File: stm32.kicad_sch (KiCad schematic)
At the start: 17 parts, among them J1 TC2030-IDC, U2 STM32F410CBU6, U3 RT9080-33GJ5

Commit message: more routing. switched to RA buttons, moved the buck closer to the barrel
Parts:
- removed C7, C8: 1uF, Capacitor_SMD:C_0402_1005Metric, symbol Device:C
- removed U3: RT9080-33GJ5, blockaxe:RT9080-33GJ5, symbol blockaxe:RT9080-33GJ5
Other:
- note removed: "STM32 3V3 LDO"
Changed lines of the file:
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@@
   (junction (at 63.5 67.945) (diameter 0) (color 0 0 0 0)
   )
-  (junction (at 73.025 24.13) (diameter 0) (color 0 0 0 0)
-  )
-  (junction (at 34.925 24.13) (diameter 0) (color 0 0 0 0)
-  )
   (junction (at 189.23 55.88) (diameter 0) (color 0 0 0 0)
   )
@@
   (junction (at 203.2 55.88) (diameter 0) (color 0 0 0 0)
   )
-  (junction (at 43.815 24.13) (diameter 0) (color 0 0 0 0)
-  )
   (junction (at 136.525 60.325) (diameter 0) (color 0 0 0 0)
   )
-  (junction (at 66.675 37.465) (diameter 0) (color 0 0 0 0)
-  )
   (junction (at 203.2 69.215) (diameter 0) (color 0 0 0 0)
   )
@@
     (stroke (width 0) (type default))
   )
-  (wire (pts (xy 64.135 24.13) (xy 73.025 24.13))
-    (stroke (width 0) (type default))
-  )
   (wire (pts (xy 63.5 79.375) (xy 63.5 81.28))
     (stroke (width 0) (type default))
@@
     (stroke (width 0) (type default))
   )
-  (wire (pts (xy 73.025 24.13) (xy 73.025 26.67))
-    (stroke (width 0) (type default))
-  )
   (wire (pts (xy 145.415 62.865) (xy 145.415 65.405))
     (stroke (width 0) (type default))
@@
     (stroke (width 0) (type default))
   )
-  (wire (pts (xy 27.305 24.13) (xy 34.925 24.13))
-    (stroke (width 0) (type default))
-  )
-  (wire (pts (xy 34.925 37.465) (xy 34.925 34.29))
-    (stroke (width 0) (type default))
-  )
   (wire (pts (xy 77.47 79.375) (xy 77.47 81.28))
     (stroke (width 0) (type default))
@@
     (stroke (width 0) (type default))
   )
-  (wire (pts (xy 73.025 37.465) (xy 66.675 37.465))
-    (stroke (width 0) (type default))
-  )
   (wire (pts (xy 215.9 66.04) (xy 215.9 69.215))
     (stroke (width 0) (type default))
@@
     (stroke (width 0) (type default))
   )
-  (wire (pts (xy 66.675 26.67) (xy 66.675 37.465))
-    (stroke (width 0) (type default))
-  )
-  (wire (pts (xy 46.355 26.67) (xy 43.815 26.67))
-    (stroke (width 0) (type default))
-  )
-  (wire (pts (xy 66.675 37.465) (xy 34.925 37.465))
-    (stroke (width 0) (type default))
-  )
-  (wire (pts (xy 73.025 24.13) (xy 76.835 24.13))
-    (stroke (width 0) (type default))
-  )
-  (wire (pts (xy 73.025 34.29) (xy 73.025 37.465))
-    (stroke (width 0) (type default))
-  )
   (wire (pts (xy 201.93 119.38) (xy 209.55 119.38))
     (stroke (width 0) (type default))
@@
     (stroke (width 0) (type default))
   )
-  (wire (pts (xy 34.925 24.13) (xy 34.925 26.67))
-    (stroke (width 0) (type default))
-  )
   (wire (pts (xy 117.475 139.065) (xy 140.335 139.065))
     (stroke (width 0) (type default))
   )
-  (wire (pts (xy 34.925 24.13) (xy 43.815 24.13))
-    (stroke (width 0) (type default))
-  )
   (wire (pts (xy 92.71 111.125) (xy 103.505 111.125))
     (stroke (width 0) (type default))
   )
-  (wire (pts (xy 43.815 24.13) (xy 46.355 24.13))
-    (stroke (width 0) (type default))
-  )
-  (wire (pts (xy 64.135 26.67) (xy 66.675 26.67))
-    (stroke (width 0) (type default))
-  )
   (wire (pts (xy 136.525 57.785) (xy 136.525 60.325))
     (stroke (width 0) (type default))
@@
     (stroke (width 0) (type default))
   )
-  (wire (pts (xy 43.815 26.67) (xy 43.815 24.13))
-    (stroke (width 0) (type default))
-  )
   (text "Bootloader UART ->" (at 50.165 100.33 0)
-    (effects (font (size 1.27 1.27)) (justify left bottom))
-  )
-  (text "STM32 3V3 LDO" (at 45.72 40.64 0)
     (effects (font (size 1.27 1.27)) (justify left bottom))
   )
@@
     (effects (font (size 1.27 1.27)) (justify left bottom))
   )
-  (label "5V" (at 37.465 24.13 0) (fields_autoplaced)
-    (effects (font (size 1.27 1.27)) (justify left bottom))
-  )
   (label "TX1" (at 92.71 98.425 0) (fields_autoplaced)
     (effects (font (size 1.27 1.27)) (justify left bottom))
@@
     (effects (font (size 1.27 1.27)) (justify right bottom))
   )
-  (label "GND" (at 52.705 37.465 0) (fields_autoplaced)
-    (effects (font (size 1.27 1.27)) (justify left bottom))
-  )
   (label "GND" (at 117.475 139.065 0) (fields_autoplaced)
     (effects (font (size 1.27 1.27)) (justify left bottom))
@@
   (label "RESET" (at 65.405 67.945 0) (fields_autoplaced)
     (effects (font (size 1.27 1.27)) (justify left bottom))
-  )
-  (label "3V3" (at 76.835 24.13 180) (fields_autoplaced)
-    (effects (font (size 1.27 1.27)) (justify right bottom))
   )
   (label "3V3" (at 143.51 60.325 180) (fields_autoplaced)
@@
     )
   )
-  (hierarchical_label "5V" (shape input) (at 27.305 24.13 180) (fields_autoplaced)
-    (effects (font (size 1.27 1.27)) (justify right))
-  )
   (hierarchical_label "RESET" (shape output) (at 92.71 93.345 180) (fields_autoplaced)
     (effects (font (size 1.27 1.27)) (justify right))
@@
   )
   (hierarchical_label "TX-ESP32" (shape output) (at 92.71 98.425 180) (fields_autoplaced)
+    (effects (font (size 1.27 1.27)) (justify right))
+  )
+  (hierarchical_label "3V3" (shape input) (at 93.98 62.865 180) (fields_autoplaced)
     (effects (font (size 1.27 1.27)) (justify right))
   )
@@
     )
   )
-  (symbol (lib_id "Device:C") (at 73.025 30.48 0) (unit 1)
-    (in_bom yes) (on_board yes) (dnp no)
-    (property "Reference" "C8" (at 74.295 28.575 0)
-      (effects (font (size 1.27 1.27)) (justify left bottom))
-    )
-    (property "Value" "1uF" (at 74.295 33.655 0)
-      (effects (font (size 1.27 1.27)) (justify left bottom))
-    )
-    (property "Footprint" "Capacitor_SMD:C_0402_1005Metric" (at 73.025 30.48 0)
-      (effects (font (size 1.27 1.27)) hide)
-    )
-    (property "Datasheet" "" (at 73.025 30.48 0)
-      (effects (font (size 1.27 1.27)) hide)
-    )
-    (property "DK" "587-5514-1-ND" (at 73.025 30.48 0)
-      (effects (font (size 1.778 1.5113)) (justify left bottom) hide)
-    )
-    (property "PARTNO" "EMK105BJ105MV-F" (at 73.025 30.48 0)
-      (effects (font (size 1.27 1.27)) hide)
-    )
-    (pin "1")
-    (pin "2")
-    (instances
-      (project "blockaxe1"
-        (path "/a166cb37-4e3a-4be5-b2da-277a3281a4de"
-          (reference "C8") (unit 1)
-        )
-        (path "/a166cb37-4e3a-4be5-b2da-277a3281a4de/a2f53eaa-4b17-468c-8132-e21e20b70349"
-          (reference "C28") (unit 1)
-        )
-      )
-      (project "esp32"
-        (path "/dcd2fc1c-da48-40a9-b97c-5712d9530f4f"
-          (reference "C49") (unit 1)
-        )
-      )
-      (project "bitaxeUltra"
-        (path "/e63e39d7-6ac0-4ffd-8aa3-1841a4541b55/ca857324-2ec8-447e-bd58-90d0c2e6b6d7"
-          (reference "C49") (unit 1)
-        )
-      )
-    )
-  )
   (symbol (lib_id "Device:R_US") (at 63.5 61.595 180) (unit 1)
     (in_bom yes) (on_board yes) (dnp no) (fields_autoplaced)
@@
         (path "/a166cb37-4e3a-4be5-b2da-277a3281a4de/a2f53eaa-4b17-468c-8132-e21e20b70349"
           (reference "R1") (unit 1)
-        )
-      )
-    )
-  )
-  (symbol (lib_id "blockaxe:RT9080-33GJ5") (at 55.245 25.4 0) (unit 1)
-    (in_bom yes) (on_board yes) (dnp no) (fields_autoplaced)
-    (property "Reference" "U3" (at 55.245 16.51 0)
-      (effects (font (size 1.27 1.27)))
-    )
-    (property "Value" "RT9080-33GJ5" (at 55.245 19.05 0)
-      (effects (font (size 1.27 1.27)))
-    )
-    (property "Footprint" "blockaxe:RT9080-33GJ5" (at 104.775 7.62 0)
-      (effects (font (size 1.524 1.524)) hide)
-    )
-    (property "Datasheet" "https://www.richtek.com/assets/product_file/RT9080/DS9080-05.pdf" (at 46.355 24.13 0)
-      (effects (font (size 1.524 1.524)) hide)
-    )
-    (property "DK" "1028-1509-1-ND" (at 55.245 25.4 0)
-      (effects (font (size 1.27 1.27)) hide)
-    )
-    (property "PARTNO" "RT9080-33GJ5" (at 55.245 25.4 0)
-      (effects (font (size 1.27 1.27)) hide)
-    )
-    (pin "1")
-    (pin "2")
-    (pin "3")
-    (pin "4")
-    (pin "5")
-    (instances
-      (project "blockaxe1"
-        (path "/a166cb37-4e3a-4be5-b2da-277a3281a4de"
-          (reference "U3") (unit 1)
-        )
-        (path "/a166cb37-4e3a-4be5-b2da-277a3281a4de/a2f53eaa-4b17-468c-8132-e21e20b70349"
-          (reference "U12") (unit 1)
-        )
-      )
-      (project "esp32"
-        (path "/dcd2fc1c-da48-40a9-b97c-5712d9530f4f"
-          (reference "U11") (unit 1)
-        )
-      )
-      (project "bitaxeUltra"
-        (path "/e63e39d7-6ac0-4ffd-8aa3-1841a4541b55/ca857324-2ec8-447e-bd58-90d0c2e6b6d7"
-          (reference "U11") (unit 1)
         )
       )
@@
         )
       )
-    )
-  )
-  (symbol (lib_id "Device:C") (at 34.925 30.48 0) (unit 1)
-    (in_bom yes) (on_board yes) (dnp no)
-    (property "Reference" "C7" (at 36.195 28.575 0)
-      (effects (font (size 1.27 1.27)) (justify left bottom))
-    )
-    (property "Value" "1uF" (at 36.195 33.655 0)
-      (effects (font (size 1.27 1.27)) (justify left bottom))
-    )
-    (property "Footprint" "Capacitor_SMD:C_0402_1005Metric" (at 34.925 30.48 0)
-      (effects (font (size 1.27 1.27)) hide)
-    )
-    (property "Datasheet" "" (at 34.925 30.48 0)
-      (effects (font (size 1.27 1.27)) hide)
-    )
-    (property "DK" "587-5514-1-ND" (at 34.925 30.48 0)
-      (effects (font (size 1.778 1.5113)) (justify left bottom) hide)
-    )
-    (property "PARTNO" "EMK105BJ105MV-F" (at 34.925 30.48 0)
-      (effects (font (size 1.27 1.27)) hide)
-    )
-    (pin "1")
-    (pin "2")
-    (instances
-      (project "blockaxe1"
-        (path "/a166cb37-4e3a-4be5-b2da-277a3281a4de"
-          (reference "C7") (unit 1)
-        )
-        (path "/a166cb37-4e3a-4be5-b2da-277a3281a4de/a2f53eaa-4b17-468c-8132-e21e20b70349"
-          (reference "C27") (unit 1)
-        )
-      )
-      (project "esp32"
-        (path "/dcd2fc1c-da48-40a9-b97c-5712d9530f4f"
-          (reference "C27") (unit 1)
-        )
-      )
-      (project "bitaxeUltra"
-        (path "/e63e39d7-6ac0-4ffd-8aa3-1841a4541b55/ca857324-2ec8-447e-bd58-90d0c2e6b6d7"
-          (reference "C27") (unit 1)
-        )
-      )

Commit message: finished routing. switched back to THT barrel
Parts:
- TP3, TP4, TP5, TP6: footprint TestPoint:TestPoint_Pad_D1.5mm -> TestPoint:TestPoint_Pad_D1.0mm
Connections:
- net RESET: no longer C1.1, J1.3 (Pin_3), R2.1, TP4.1, U2.7 (NRST)
- new net SWRESET: C1.1, J1.3 (Pin_3), R2.1, TP4.1, U2.7 (NRST)
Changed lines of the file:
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@@
     (effects (font (size 1.27 1.27)) (justify left bottom))
   )
-  (label "RESET" (at 180.975 116.84 0) (fields_autoplaced)
+  (label "SWRESET" (at 180.975 116.84 0) (fields_autoplaced)
     (effects (font (size 1.27 1.27)) (justify left bottom))
   )
@@
     (effects (font (size 1.27 1.27)) (justify left bottom))
   )
-  (label "RESET" (at 65.405 67.945 0) (fields_autoplaced)
+  (label "SWRESET" (at 65.405 67.945 0) (fields_autoplaced)
     (effects (font (size 1.27 1.27)) (justify left bottom))
   )
@@
       (effects (font (size 1.27 1.27)) (justify left) hide)
     )
-    (property "Footprint" "TestPoint:TestPoint_Pad_D1.5mm" (at 209.55 114.3 0)
+    (property "Footprint" "TestPoint:TestPoint_Pad_D1.0mm" (at 209.55 114.3 0)
       (effects (font (size 1.27 1.27)) hide)
     )
@@
       (effects (font (size 1.27 1.27)) (justify left) hide)
     )
-    (property "Footprint" "TestPoint:TestPoint_Pad_D1.5mm" (at 209.55 109.22 0)
+    (property "Footprint" "TestPoint:TestPoint_Pad_D1.0mm" (at 209.55 109.22 0)
       (effects (font (size 1.27 1.27)) hide)
     )
@@
       (effects (font (size 1.27 1.27)) (justify left) hide)
     )
-    (property "Footprint" "TestPoint:TestPoint_Pad_D1.5mm" (at 209.55 111.76 0)
+    (property "Footprint" "TestPoint:TestPoint_Pad_D1.0mm" (at 209.55 111.76 0)
       (effects (font (size 1.27 1.27)) hide)
     )
@@
       (effects (font (size 1.27 1.27)) (justify left) hide)
     )
-    (property "Footprint" "TestPoint:TestPoint_Pad_D1.5mm" (at 180.975 121.92 0)
-      (effects (font (size 1.27 1.27)) hide)
-    )
+    (property "Footprint" "TestPoint:TestPoint_Pad_D1.0mm" (at 180.975 121.92 0)
+      (effects (font (size 1.27 1.27)) hide)
+    )

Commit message: added gerbers and BOM
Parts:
- added J7: Conn_01x03, Connector_PinHeader_2.54mm:PinHeader_1x03_P2.54mm_Vertical, symbol Connector_Generic:Conn_01x03
- C1, C2, C3, C4, C5: DK (none) -> 1292-1639-1-ND; PARTNO (none) -> 0402X104K100CT
- C6: DK (none) -> 1276-1482-1-ND; PARTNO (none) -> CL05A475MP5NRNC
- R1, R2: DK (none) -> 311-10KJRCT-ND; PARTNO (none) -> RC0402JR-0710KL
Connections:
- net GND: now also J7.3 (Pin_3)
- net TX2: now reaches U2.12 (PA2)
- net TX2: now also J7.2 (Pin_2)
- net RX2: now reaches U2.13 (PA3)
- net RX2: now also J7.1 (Pin_1)
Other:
- note added: "STM32 Serial Debug"
- note added: "USART2"
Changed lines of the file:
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@@
+    (stroke (width 0) (type default))
+  )
+  (wire (pts (xy 92.71 80.645) (xy 103.505 80.645))
     (stroke (width 0) (type default))
   )
@@
     (stroke (width 0) (type default))
   )
+  (wire (pts (xy 179.705 91.44) (xy 189.865 91.44))
+    (stroke (width 0) (type default))
+  )
   (wire (pts (xy 189.23 69.215) (xy 175.26 69.215))
     (stroke (width 0) (type default))
   )
+  (wire (pts (xy 179.705 88.9) (xy 189.865 88.9))
+    (stroke (width 0) (type default))
+  )
   (wire (pts (xy 180.975 116.84) (xy 189.23 116.84))
     (stroke (width 0) (type default))
@@
     (stroke (width 0) (type default))
   )
+  (wire (pts (xy 179.705 86.36) (xy 189.865 86.36))
+    (stroke (width 0) (type default))
+  )
   (wire (pts (xy 103.505 67.945) (xy 63.5 67.945))
     (stroke (width 0) (type default))
@@
     (stroke (width 0) (type default))
   )
+  (wire (pts (xy 92.71 83.185) (xy 103.505 83.185))
+    (stroke (width 0) (type default))
+  )
   (wire (pts (xy 215.9 58.42) (xy 215.9 55.88))
     (stroke (width 0) (type default))
   )
+  (text "STM32 Serial Debug" (at 186.69 80.01 0)
+    (effects (font (size 1.27 1.27)) (justify left bottom))
+  )
   (text "Bootloader UART ->" (at 50.165 100.33 0)
+    (effects (font (size 1.27 1.27)) (justify left bottom))
+  )
+  (text "USART2" (at 191.77 82.55 0)
     (effects (font (size 1.27 1.27)) (justify left bottom))
   )
@@
     (effects (font (size 1.27 1.27)) (justify left bottom))
   )
+  (label "TX2" (at 92.71 80.645 0) (fields_autoplaced)
+    (effects (font (size 1.27 1.27)) (justify left bottom))
+  )
   (label "SWCLK" (at 92.71 111.125 0) (fields_autoplaced)
     (effects (font (size 1.27 1.27)) (justify left bottom))
   )
+  (label "RX2" (at 179.705 86.36 0) (fields_autoplaced)
+    (effects (font (size 1.27 1.27)) (justify left bottom))
+  )
   (label "SWRESET" (at 65.405 67.945 0) (fields_autoplaced)
+    (effects (font (size 1.27 1.27)) (justify left bottom))
+  )
+  (label "TX2" (at 179.705 88.9 0) (fields_autoplaced)
     (effects (font (size 1.27 1.27)) (justify left bottom))
   )
@@
   )
   (label "RX1" (at 92.71 100.965 0) (fields_autoplaced)
+    (effects (font (size 1.27 1.27)) (justify left bottom))
+  )
+  (label "GND" (at 179.705 91.44 0) (fields_autoplaced)
+    (effects (font (size 1.27 1.27)) (justify left bottom))
+  )
+  (label "RX2" (at 92.71 83.185 0) (fields_autoplaced)
     (effects (font (size 1.27 1.27)) (justify left bottom))
   )
@@
       (effects (font (size 1.27 1.27)) hide)
     )
+    (property "DK" "1292-1639-1-ND" (at 189.23 62.23 0)
+      (effects (font (size 1.27 1.27)) hide)
+    )
+    (property "PARTNO" "0402X104K100CT" (at 189.23 62.23 0)
+      (effects (font (size 1.27 1.27)) hide)
+    )
     (pin "1")
     (pin "2")
@@
       (effects (font (size 1.27 1.27)) hide)
     )
+    (property "DK" "1276-1482-1-ND" (at 145.415 69.215 0)
+      (effects (font (size 1.27 1.27)) hide)
+    )
+    (property "PARTNO" "CL05A475MP5NRNC" (at 145.415 69.215 0)
+      (effects (font (size 1.27 1.27)) hide)
+    )
     (pin "1")
     (pin "2")
@@
         (path "/a166cb37-4e3a-4be5-b2da-277a3281a4de/a2f53eaa-4b17-468c-8132-e21e20b70349"
           (reference "C2") (unit 1)
+        )
+      )
+    )
+  )
+  (symbol (lib_id "Connector_Generic:Conn_01x03") (at 194.945 88.9 0) (unit 1)
+    (in_bom yes) (on_board yes) (dnp no) (fields_autoplaced)
+    (property "Reference" "J7" (at 198.12 87.63 0)
+      (effects (font (size 1.27 1.27)) (justify left))
+    )
+    (property "Value" "Conn_01x03" (at 198.12 90.17 0)
+      (effects (font (size 1.27 1.27)) (justify left))
+    )
+    (property "Footprint" "Connector_PinHeader_2.54mm:PinHeader_1x03_P2.54mm_Vertical" (at 194.945 88.9 0)
+      (effects (font (size 1.27 1.27)) hide)
+    )
+    (property "Datasheet" "~" (at 194.945 88.9 0)
+      (effects (font (size 1.27 1.27)) hide)
+    )
+    (pin "2")
+    (pin "1")
+    (pin "3")
+    (instances
+      (project "blockaxe1"
+        (path "/a166cb37-4e3a-4be5-b2da-277a3281a4de/a2f53eaa-4b17-468c-8132-e21e20b70349"
+          (reference "J7") (unit 1)
         )
       )
@@
     )
     (property "Datasheet" "~" (at 175.26 62.23 0)
+      (effects (font (size 1.27 1.27)) hide)
+    )
+    (property "DK" "1292-1639-1-ND" (at 175.26 62.23 0)
+      (effects (font (size 1.27 1.27)) hide)
+    )
+    (property "PARTNO" "0402X104K100CT" (at 175.26 62.23 0)
       (effects (font (size 1.27 1.27)) hide)
     )
@@
       (effects (font (size 1.27 1.27)) hide)
     )
+    (property "DK" "1292-1639-1-ND" (at 203.2 62.23 0)
+      (effects (font (size 1.27 1.27)) hide)
+    )
+    (property "PARTNO" "0402X104K100CT" (at 203.2 62.23 0)
+      (effects (font (size 1.27 1.27)) hide)
+    )
     (pin "1")
     (pin "2")
@@
       (effects (font (size 1.27 1.27)) hide)
     )
+    (property "DK" "311-10KJRCT-ND" (at 63.5 61.595 0)
+      (effects (font (size 1.27 1.27)) hide)
+    )
+    (property "PARTNO" "RC0402JR-0710KL" (at 63.5 61.595 0)
+      (effects (font (size 1.27 1.27)) hide)
+    )
     (pin "1")
     (pin "2")
@@
       (effects (font (size 1.27 1.27)) hide)
     )
+    (property "DK" "311-10KJRCT-ND" (at 77.47 75.565 0)
+      (effects (font (size 1.27 1.27)) hide)
+    )
+    (property "PARTNO" "RC0402JR-0710KL" (at 77.47 75.565 0)
+      (effects (font (size 1.27 1.27)) hide)
+    )
     (pin "1")
     (pin "2")
@@
     )
     (property "Datasheet" "~" (at 63.5 75.565 0)
+      (effects (font (size 1.27 1.27)) hide)
+    )
+    (property "DK" "1292-1639-1-ND" (at 63.5 75.565 0)
+      (effects (font (size 1.27 1.27)) hide)
+    )
+    (property "PARTNO" "0402X104K100CT" (at 63.5 75.565 0)
       (effects (font (size 1.27 1.27)) hide)
     )
@@
       (effects (font (size 1.27 1.27)) hide)
     )
+    (property "DK" "1292-1639-1-ND" (at 215.9 62.23 0)
+      (effects (font (size 1.27 1.27)) hide)
+    )
+    (property "PARTNO" "0402X104K100CT" (at 215.9 62.23 0)
+      (effects (font (size 1.27 1.27)) hide)
+    )

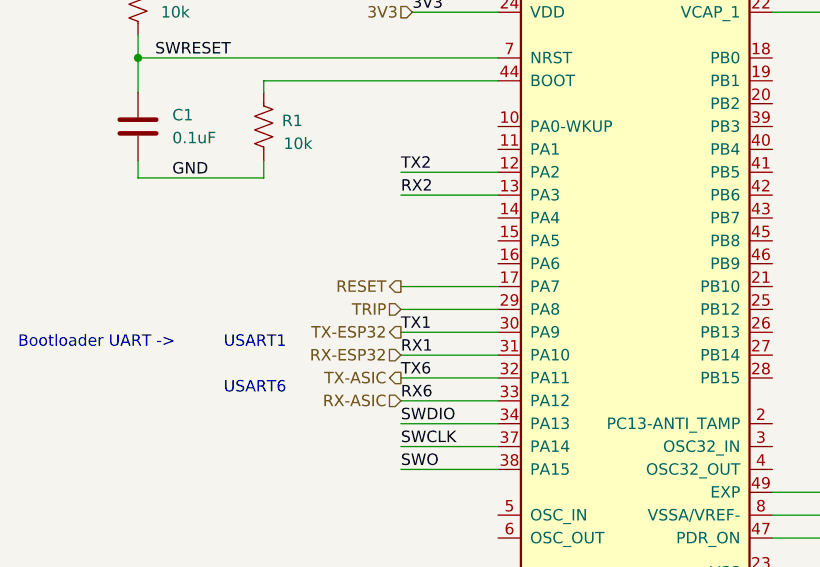
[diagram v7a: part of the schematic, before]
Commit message: Switching to 1.2V Oscillator for #3 Switch the level shifter for #4
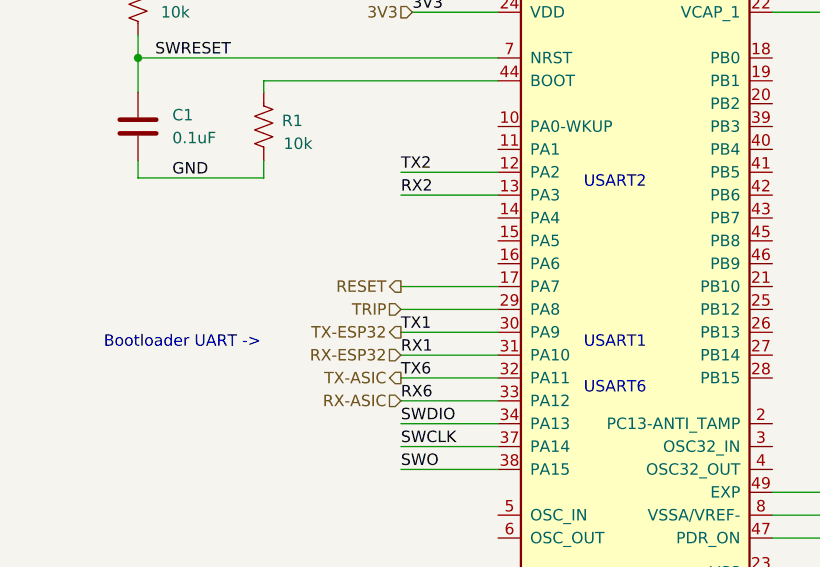
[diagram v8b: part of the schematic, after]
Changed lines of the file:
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@@
     (stroke (width 0) (type default))
+  )
+  (text "USART2" (at 113.03 82.55 0)
+    (effects (font (size 1.27 1.27)) (justify left bottom))
   )
   (text "STM32 Serial Debug" (at 186.69 80.01 0)
     (effects (font (size 1.27 1.27)) (justify left bottom))
   )
-  (text "Bootloader UART ->" (at 50.165 100.33 0)
+  (text "Bootloader UART ->" (at 59.69 100.33 0)
     (effects (font (size 1.27 1.27)) (justify left bottom))
   )
@@
     (effects (font (size 1.27 1.27)) (justify left bottom))
   )
-  (text "USART1" (at 73.025 100.33 0)
+  (text "USART1" (at 113.03 100.33 0)
     (effects (font (size 1.27 1.27)) (justify left bottom))
   )
-  (text "USART6" (at 73.025 105.41 0)
+  (text "USART6" (at 113.03 105.41 0)
     (effects (font (size 1.27 1.27)) (justify left bottom))
   )
